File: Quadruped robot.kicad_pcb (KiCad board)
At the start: 2 copper layers, 100 x 130 mm, 5 parts, among them J1 Screw_Terminal_01x04, J2 Screw_Terminal_01x03, J3 Screw_Terminal_01x20, J4 Screw_Terminal_01x17, U1 ESP32-S3-DEVKITC-1-N8R2

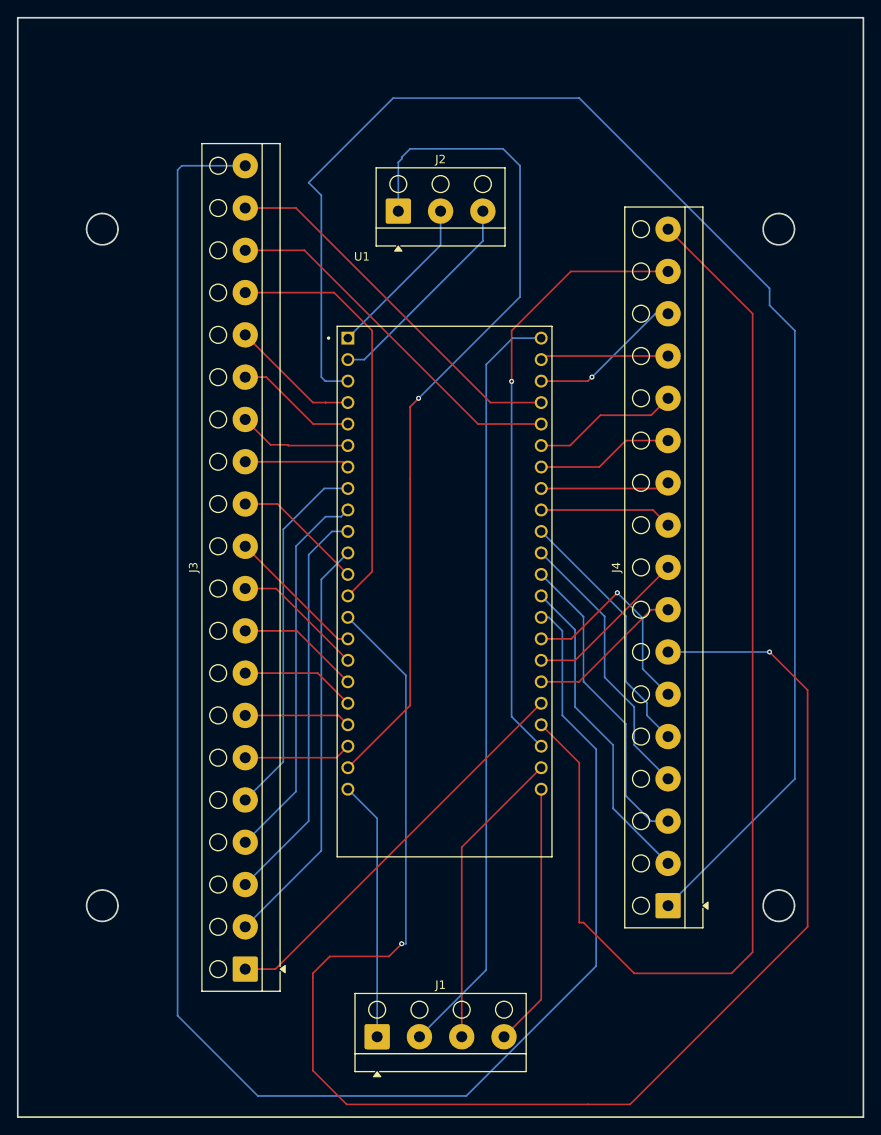
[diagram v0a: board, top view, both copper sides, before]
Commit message: Adding text to pcb
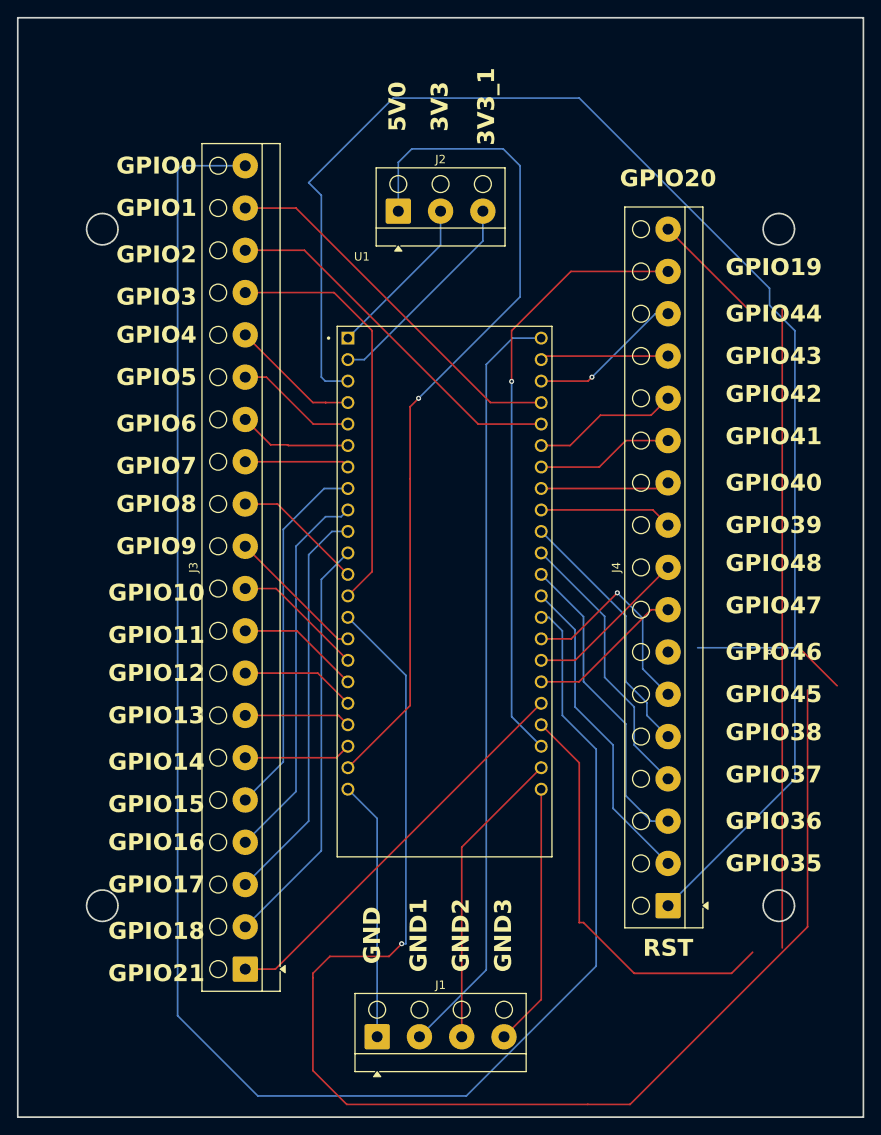
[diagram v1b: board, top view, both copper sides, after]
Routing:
- net Net-(J4-Pin_7): track 180.6 -> 168.6 mm
- net Net-(J4-Pin_1): track 175.4 -> 187.4 mm
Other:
- board text added: "3V3"
- board text added: "3V3_1"
- board text added: "5V0"
- board text added: "GND"
- board text added: "GND1"
- board text added: "GND2"
- board text added: "GND3"
- board text added: "GPIO0"
- board text added: "GPIO1"
- board text added: "GPIO10"
- board text added: "GPIO11"
- board text added: "GPIO12"
- board text added: "GPIO13"
- board text added: "GPIO14"
- board text added: "GPIO15"
- board text added: "GPIO16"
- board text added: "GPIO17"
- board text added: "GPIO18"
- board text added: "GPIO19"
- board text added: "GPIO2"
- board text added: "GPIO20"
- board text added: "GPIO21"
- board text added: "GPIO3"
- board text added: "GPIO35"
- board text added: "GPIO36"
- board text added: "GPIO37"
- board text added: "GPIO38"
- board text added: "GPIO39"
- board text added: "GPIO4"
- board text added: "GPIO40"
- board text added: "GPIO41"
- board text added: "GPIO42"
- board text added: "GPIO43"
- board text added: "GPIO44"
- board text added: "GPIO45"
- board text added: "GPIO46"
- board text added: "GPIO47"
- board text added: "GPIO48"
- board text added: "GPIO5"
- board text added: "GPIO6"
- board text added: "GPIO7"
- board text added: "GPIO8"
- board text added: "GPIO9"
- board text added: "RST"
